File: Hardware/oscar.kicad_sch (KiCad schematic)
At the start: 51 parts, among them J1 SWD_Header, J2 ChannelA_In, J3 ChannelB_In, J4 ChannelC_In, J5 ChA_Buff_Out, J6 ChB_Buff_Out, J7 ChC_Buff_Out, J8 MIDI_In, J9 Eurorack_10_pin_power, SW1 Left_Encoder, SW2 Right_Encoder, SW3 SW_Push, U1 STM32F446RETx, U2 ILI9341_SPI_Daughterboard, U3 MCP6004, U4 TL074, U5 LM1117-3.3, Y1 Crystal

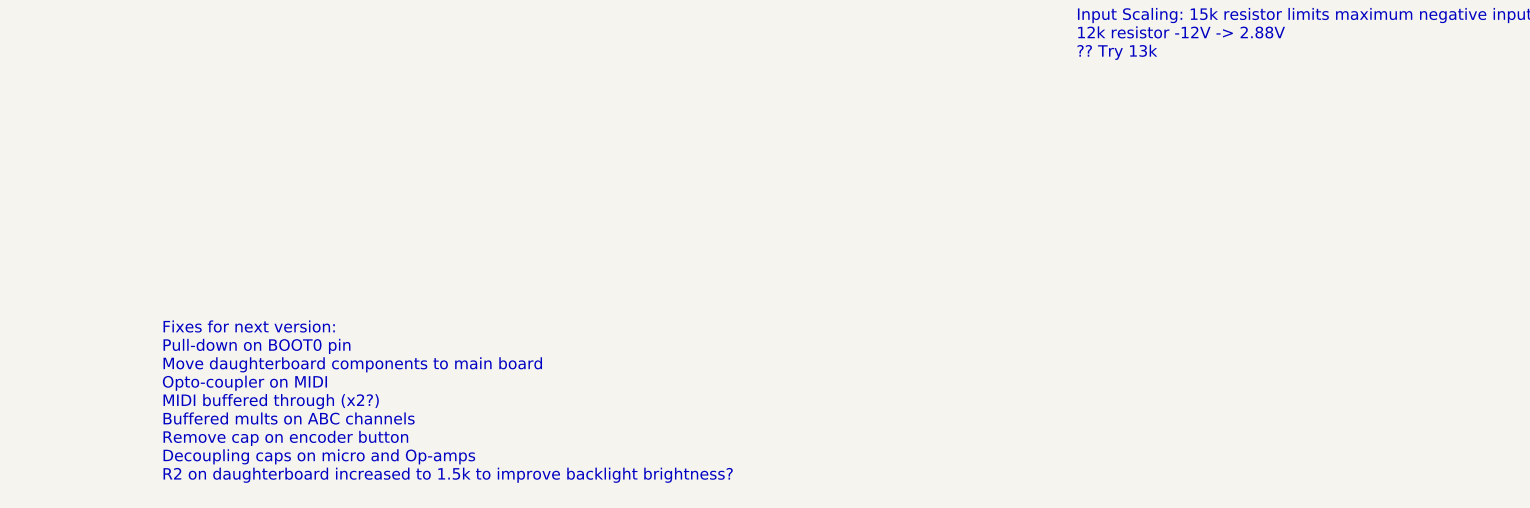
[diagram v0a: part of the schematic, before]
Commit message: Update notes in schematic
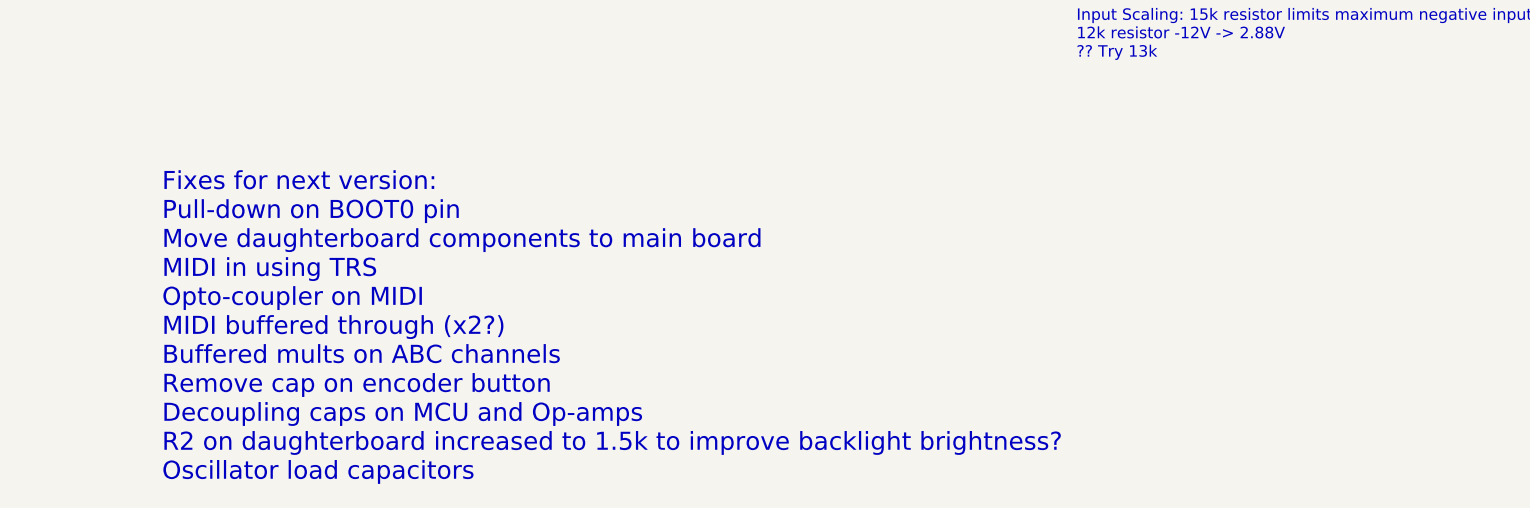
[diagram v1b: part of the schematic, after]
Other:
- note added: "Fixes for next version: Pull-down on BOOT0 pin Move daughterboard components to main board MIDI in using TRS Opto-coupler on MIDI MIDI buffered through (x2?) Buffered mults on ABC channels Remove cap on encoder button Decoupling caps on MCU and Op-amps R2 on daughterboard increased to 1.5k to improve backlight brightness? Oscillator load capacitors"
- note removed: "Fixes for next version: Pull-down on BOOT0 pin Move daughterboard components to main board Opto-coupler on MIDI MIDI buffered through (x2?) Buffered mults on ABC channels Remove cap on encoder button Decoupling caps on micro and Op-amps R2 on daughterboard increased to 1.5k to improve backlight brightness?"
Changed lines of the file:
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@@
     (effects (font (size 1.27 1.27)) (justify left bottom))
   )
-  (text "Fixes for next version:\nPull-down on BOOT0 pin\nMove daughterboard components to main board\nOpto-coupler on MIDI\nMIDI buffered through (x2?)\nBuffered mults on ABC channels\nRemove cap on encoder button\nDecoupling caps on micro and Op-amps\nR2 on daughterboard increased to 1.5k to improve backlight brightness?"
+  (text "Fixes for next version:\nPull-down on BOOT0 pin\nMove daughterboard components to main board\nMIDI in using TRS\nOpto-coupler on MIDI\nMIDI buffered through (x2?)\nBuffered mults on ABC channels\nRemove cap on encoder button\nDecoupling caps on MCU and Op-amps\nR2 on daughterboard increased to 1.5k to improve backlight brightness?\nOscillator load capacitors"
     (at 43.18 255.27 0)
-    (effects (font (size 1.27 1.27)) (justify left bottom))
+    (effects (font (size 2 2)) (justify left bottom))
   )
   (text "Power Sections" (at 287.02 198.12 0)
